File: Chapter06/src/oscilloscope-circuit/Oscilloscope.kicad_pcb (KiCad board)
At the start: 4 copper layers, 63.5 x 63.5 mm, 84 parts, among them J1 Ch1 BNC, J2 PMOD B, J3 PMOD C, J4 SPI header, J5 1 KHz ±3.0V, J6 GND, J7 3.0VDC, J8 -3.0VDC, U1 LTC2267-14, U2 TLV75718PDBV, U3 MIC5501-3.0YM5, U4 LM2776, U5 TC59, U6 GDT CG775, U7 ADA4817-1, U8 LT6411, U9 TLV2371DBV

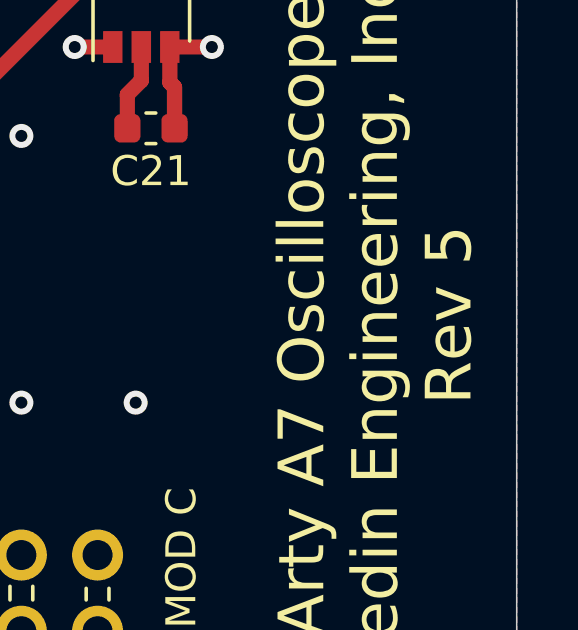
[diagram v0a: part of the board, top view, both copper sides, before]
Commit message: Added chapters 9 and 10
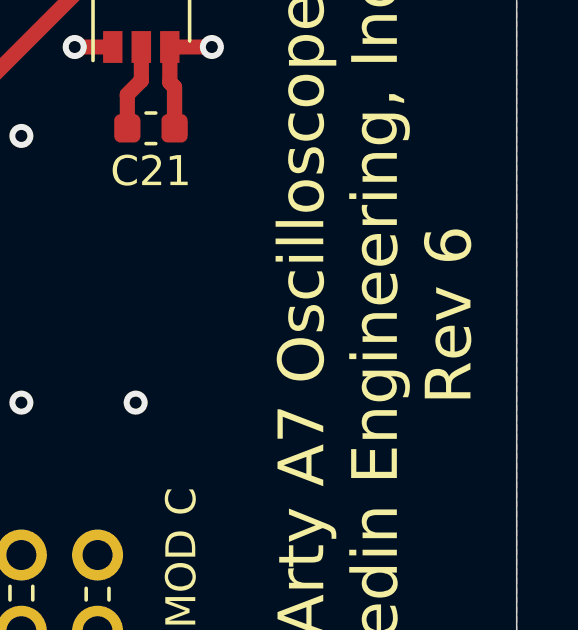
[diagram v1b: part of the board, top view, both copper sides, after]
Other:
- board text added: "Arty A7 Oscilloscope Ledin Engineering, Inc. Rev 6"
- board text removed: "Arty A7 Oscilloscope Ledin Engineering, Inc. Rev 5"
